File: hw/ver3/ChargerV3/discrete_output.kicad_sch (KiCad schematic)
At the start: 20 parts, among them Q12 BSS138, Q13 BSS138, Q14 BSS138, Q15 BSS84, Q16 BSS138, Q28 BSS138, U14 74HC595, U15 74HC595

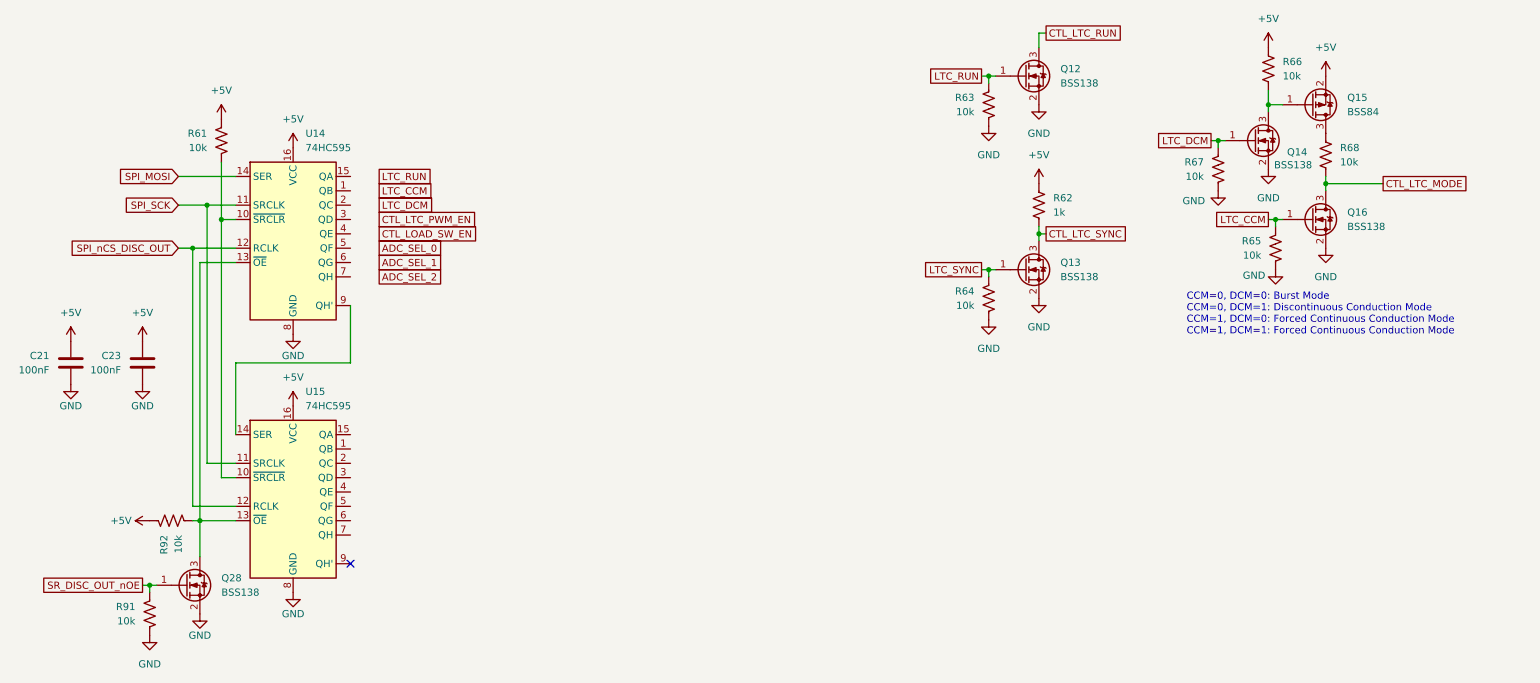
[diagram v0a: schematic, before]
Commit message: Redo some charger routing. Improve design for interconnect
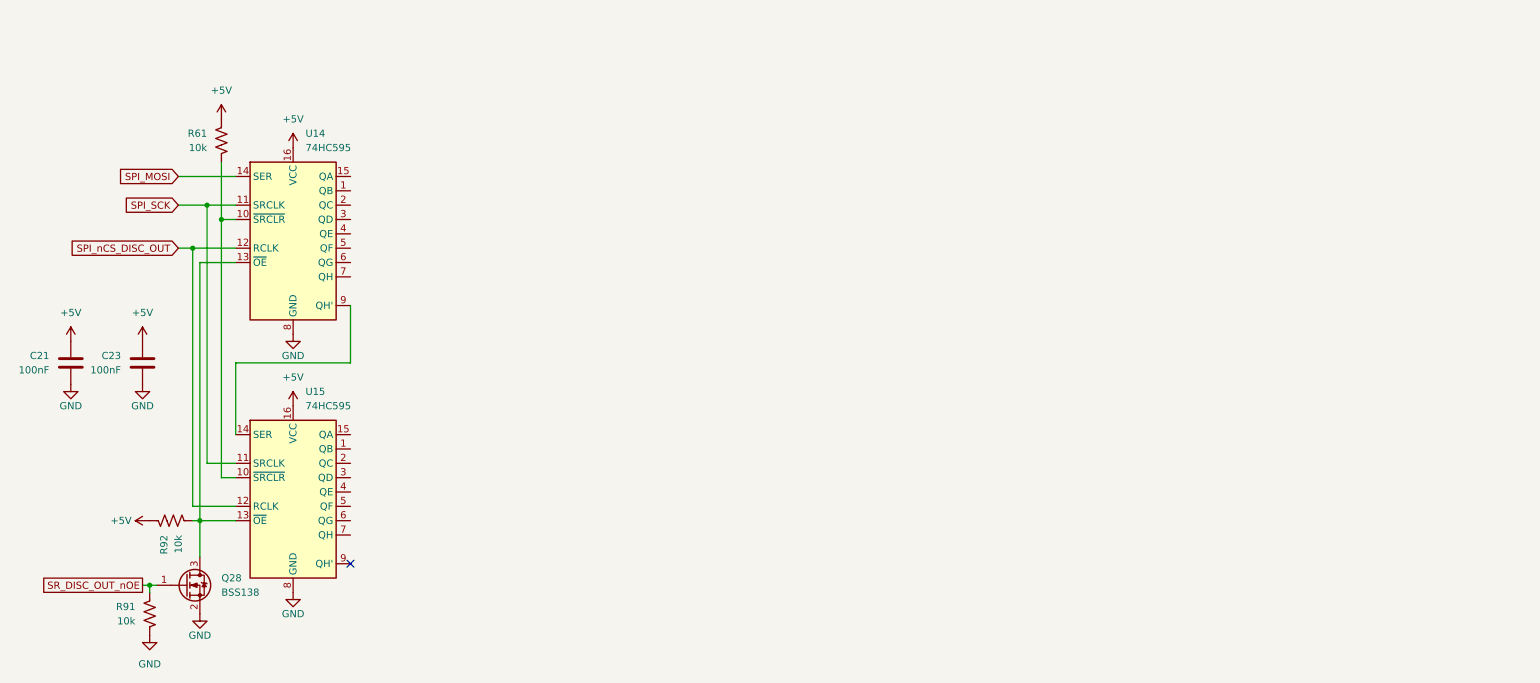
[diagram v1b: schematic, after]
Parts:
- removed Q12, Q13, Q14, Q16: BSS138, Package_TO_SOT_SMD:SOT-23, symbol Transistor_FET:BSS138
- removed Q15: BSS84, Package_TO_SOT_SMD:SOT-23, symbol Transistor_FET:BSS84
- removed R62: 1k, Resistor_SMD:R_0603_1608Metric, symbol Device:R_US
- removed R63, R64, R65, R66, R67, R68: 10k, Resistor_SMD:R_0603_1608Metric, symbol Device:R_US
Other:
- note removed: "CCM=0, DCM=0: Burst Mode CCM=0, DCM=1: Discontinuous Conduction Mode CCM=1, DCM=0: Forced Continuous Conduction Mode CCM=1, DCM=1: Forced Continuous Conduction Mode"
